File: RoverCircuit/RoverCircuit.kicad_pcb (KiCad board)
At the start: 2 copper layers, 11 parts, among them J1 PIC24_JST_1-10, J2 PIC24_JST_11-20, J3 Servo_JST, J4 Left_Wheel_JST, J5 Right_Wheel_JST, J6 Battery_Terminal, Q1 NMOS, Q2 PMOS, U1 LM2596S-5

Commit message: Added Sharp Sensors to KiCad
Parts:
- removed U1: LM2596S-5, Package_TO_SOT_SMD:TO-263-5_TabPin3
- added D1: LED, LED_THT:LED_D8.0mm, F.Cu at (77.8, 41.0)
- added D2: LED, LED_THT:LED_D8.0mm, F.Cu at (77.8, 51.7)
- added D3: LED, LED_THT:LED_D8.0mm, F.Cu at (77.8, 62.3)
- added D4: LED, LED_THT:LED_D8.0mm, F.Cu at (77.8, 73.0)
- added J10: Front_Sharp_Sensor_JST, Connector_JST:JST_EH_B3B-EH-A_1x03_P2.50mm_Vertical, F.Cu at (54.3, 54.2)
- added J7: Voltage_Regulator_JST, Connector_JST:JST_EH_B3B-EH-A_1x03_P2.50mm_Vertical, F.Cu at (87.9, 54.5)
- added J8: Left_Sharp_Sensor_JST, Connector_JST:JST_EH_B3B-EH-A_1x03_P2.50mm_Vertical, F.Cu at (54.3, 42.5)
- added J9: Right_Sharp_Sensor_JST, Connector_JST:JST_EH_B3B-EH-A_1x03_P2.50mm_Vertical, F.Cu at (54.3, 48.4)
- added R3: 330, Resistor_THT:R_Axial_DIN0207_L6.3mm_D2.5mm_P10.16mm_Horizontal, F.Cu at (85.9, 37.7)
- added R4: 330, Resistor_THT:R_Axial_DIN0207_L6.3mm_D2.5mm_P10.16mm_Horizontal, F.Cu at (85.9, 41.7)
- added R5: 330, Resistor_THT:R_Axial_DIN0207_L6.3mm_D2.5mm_P10.16mm_Horizontal, F.Cu at (85.9, 45.8)
- added R6: 330, Resistor_THT:R_Axial_DIN0207_L6.3mm_D2.5mm_P10.16mm_Horizontal, F.Cu at (85.9, 49.8)
- J6: footprint Connector_Phoenix_SPT:PhoenixContact_SPT_5_1-H-7.5_1x01_P7.5mm_Horizontal -> TerminalBlock_CUI:TerminalBlock_CUI_TB007-508-02_1x02_P5.08mm_Horizontal
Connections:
- J1 pad 1: unconnected-(J1-Pin_1-Pad1) -> Net-(J1-Pin_1)

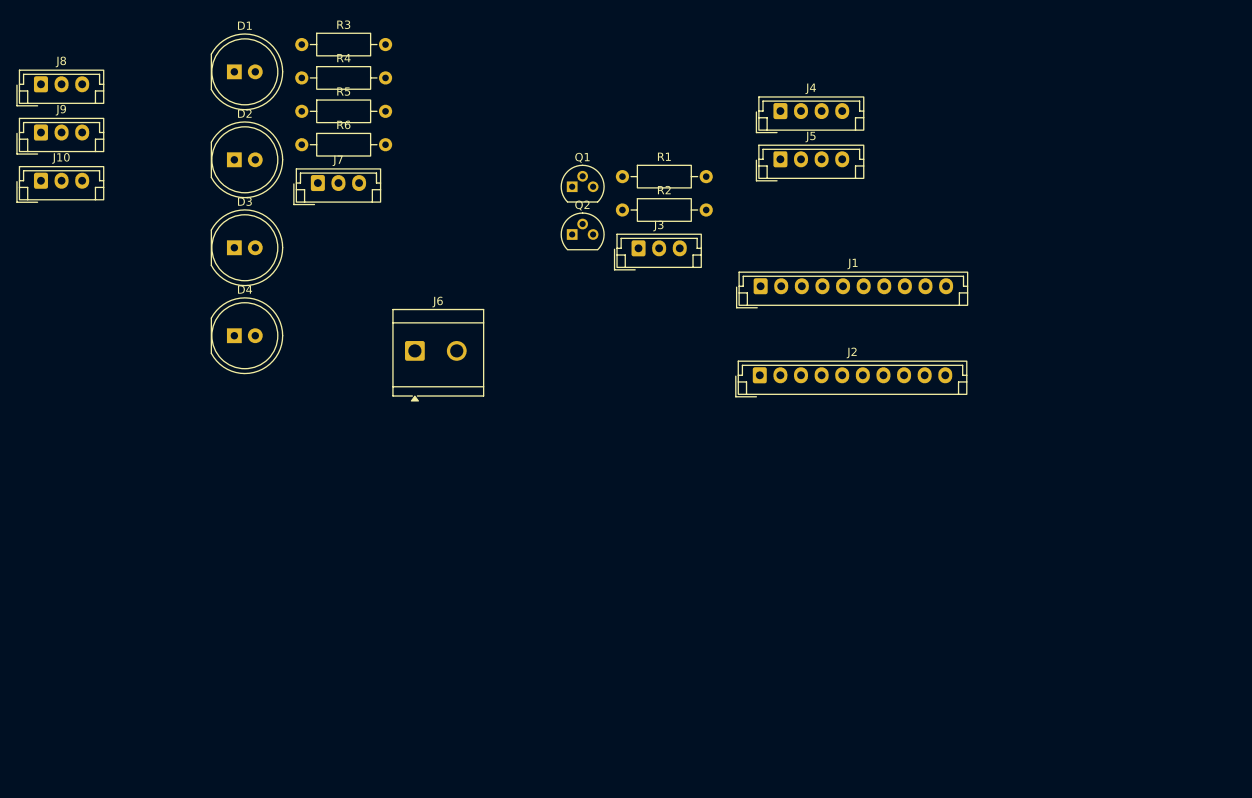
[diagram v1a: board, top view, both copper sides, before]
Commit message: Finalized rover circuit schematic, first version of QRD circuit
rover circuit layout and traces not finished yet
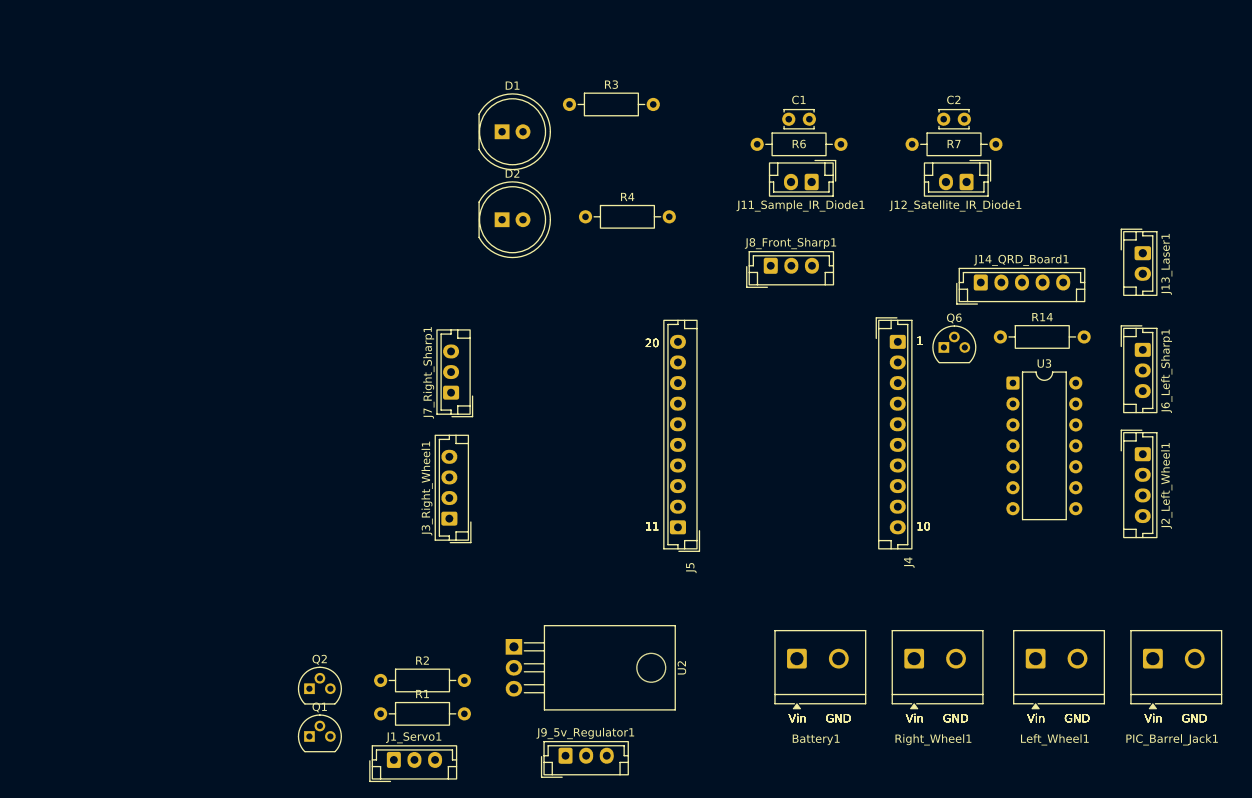
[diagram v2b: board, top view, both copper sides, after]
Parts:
- removed D3, D4: LED, LED_THT:LED_D8.0mm
- removed R5: 330, Resistor_THT:R_Axial_DIN0207_L6.3mm_D2.5mm_P10.16mm_Horizontal
- added C1: 0.1uF, Capacitor_THT:C_Disc_D3.4mm_W2.1mm_P2.50mm, F.Cu at (145.0, 46.7)
- added C2: 0.1uF, Capacitor_THT:C_Disc_D3.4mm_W2.1mm_P2.50mm, F.Cu at (163.8, 46.7)
- added J11_Sample_IR_Diode1: JST_2Pin_P2.54_V, Connector_JST:JST_EH_B2B-EH-A_1x02_P2.50mm_Vertical, F.Cu at (147.8, 54.4)
- added J12_Satellite_IR_Diode1: JST_2Pin_P2.54_V, Connector_JST:JST_EH_B2B-EH-A_1x02_P2.50mm_Vertical, F.Cu at (166.6, 54.4)
- added J13_Laser1: JST_2Pin_P2.54_V, Connector_JST:JST_EH_B2B-EH-A_1x02_P2.50mm_Vertical, F.Cu at (188.0, 63.0)
- added J14_QRD_Board1: JST_5Pin_P2.54_V, Connector_JST:JST_EH_B5B-EH-A_1x05_P2.50mm_Vertical, F.Cu at (168.3, 66.5)
- added Left_Wheel1: Left_Wheel_Power_Terminal, Custom_Library:screw_terminal, F.Cu at (177.7, 112.5)
- added PIC_Barrel_Jack1: PIC_Power_Terminal, Custom_Library:screw_terminal, F.Cu at (191.9, 112.5)
- added Q6: NMOS, Package_TO_SOT_THT:TO-92, F.Cu at (163.8, 74.4)
- added R14: 10kΩ, Resistor_THT:R_Axial_DIN0207_L6.3mm_D2.5mm_P10.16mm_Horizontal, F.Cu at (170.7, 73.2)
- added R7: 1MΩ, Resistor_THT:R_Axial_DIN0207_L6.3mm_D2.5mm_P10.16mm_Horizontal, F.Cu at (160.0, 49.8)
- added Right_Wheel1: Right_Wheel_Terminal, Custom_Library:screw_terminal, F.Cu at (162.9, 112.5)
- added U2: LM1117T-3.3, Package_TO_SOT_THT:TO-220-3_Horizontal_TabDown, F.Cu at (111.7, 110.7)
- added U3: LM324, Package_DIP:DIP-14_W7.62mm, F.Cu at (172.2, 78.7)
- Battery1: renamed from J6; footprint TerminalBlock_CUI:TerminalBlock_CUI_TB007-508-02_1x02_P5.08mm_Horizontal -> Custom_Library:screw_terminal
- J1_Servo1: renamed from J3; value Servo_JST -> JST_3Pin_P2.54_V
- J2_Left_Wheel1: renamed from J4; value Left_Wheel_JST -> JST_4Pin_P2.54_V
- J3_Right_Wheel1: renamed from J5; value Right_Wheel_JST -> JST_4Pin_P2.54_V
- J4: renamed from J1; value PIC24_JST_1-10 -> JST_10Pin_P2.54_V
- J5: renamed from J2; value PIC24_JST_11-20 -> JST_10Pin_P2.54_V
- J6_Left_Sharp1: renamed from J8; value Left_Sharp_Sensor_JST -> JST_3Pin_P2.54_V
- J7_Right_Sharp1: renamed from J9; value Right_Sharp_Sensor_JST -> JST_3Pin_P2.54_V
- J8_Front_Sharp1: renamed from J10; value Front_Sharp_Sensor_JST -> JST_3Pin_P2.54_V
- J9_5v_Regulator1: renamed from J7; value Voltage_Regulator_JST -> JST_3Pin_P2.54_V
- R6: value 330 -> 1MΩ
- moved J6_Left_Sharp1 137.5 mm to (188.0, 74.7), turned to -90 degrees
- moved J8_Front_Sharp1 89.1 mm to (142.8, 64.5)
- moved J9_5v_Regulator1 75.7 mm to (117.9, 124.0)
- moved J1_Servo1 68.8 mm to (97.1, 124.5)
- moved Q1 68.7 mm to (86.9, 121.6)
- moved Q2 68.7 mm to (86.9, 115.8)
- moved R1 67.8 mm to (95.5, 118.9)
- moved R2 67.8 mm to (95.5, 114.8)
- moved Battery1 61.9 mm to (148.7, 112.5)
- moved J2_Left_Wheel1 60.5 mm to (188.0, 87.4), turned to -90 degrees
- moved J3_Right_Wheel1 59.3 mm to (103.8, 95.2), turned to 90 degrees
- moved J7_Right_Sharp1 58.9 mm to (104.0, 79.9), turned to 90 degrees
- moved R6 55.2 mm to (141.2, 49.8)
- moved R4 38.3 mm to (120.4, 58.6)
- moved D1 33.3 mm to (110.2, 48.3)
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- renumbered Q2 to Q1, Q1 to Q2, R2 to R1, R1 to R2
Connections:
- net +3V3 renamed Net-(J5-Pin_10)
- Battery1 pad 1: /9v_Rail -> Net-(Battery1-Pin_1)
- J4 pad 10: /Debug_LED_3 -> /Debug_LED_2
- J4 pad 8: /Debug_LED_1 -> /Right_Of_Line_QRD_Input
- J4 pad 9: /Debug_LED_2 -> /Debug_LED_1
- J5 pad 11: /Debug_LED_4 -> /Laser_Output
- J9_5v_Regulator1 pad 2: /9v_Rail -> /12v_Rail
- R6 pad 1: GND -> Net-(J11_Sample_IR_Diode1-Pin_1)
- R6 pad 2: Net-(D4-K) -> /Sample_Collection_IR_Input
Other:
- board text added: "1"
- board text added: "10"
- board text added: "11"
- board text added: "20"
- board text added: "GND"
- board text added: "Vin"

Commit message: Added low pass filters on every analog input
Used R=150, C=0.1uF to attenuate frequencies above the frequency of how fast the AD converter will read each signal.
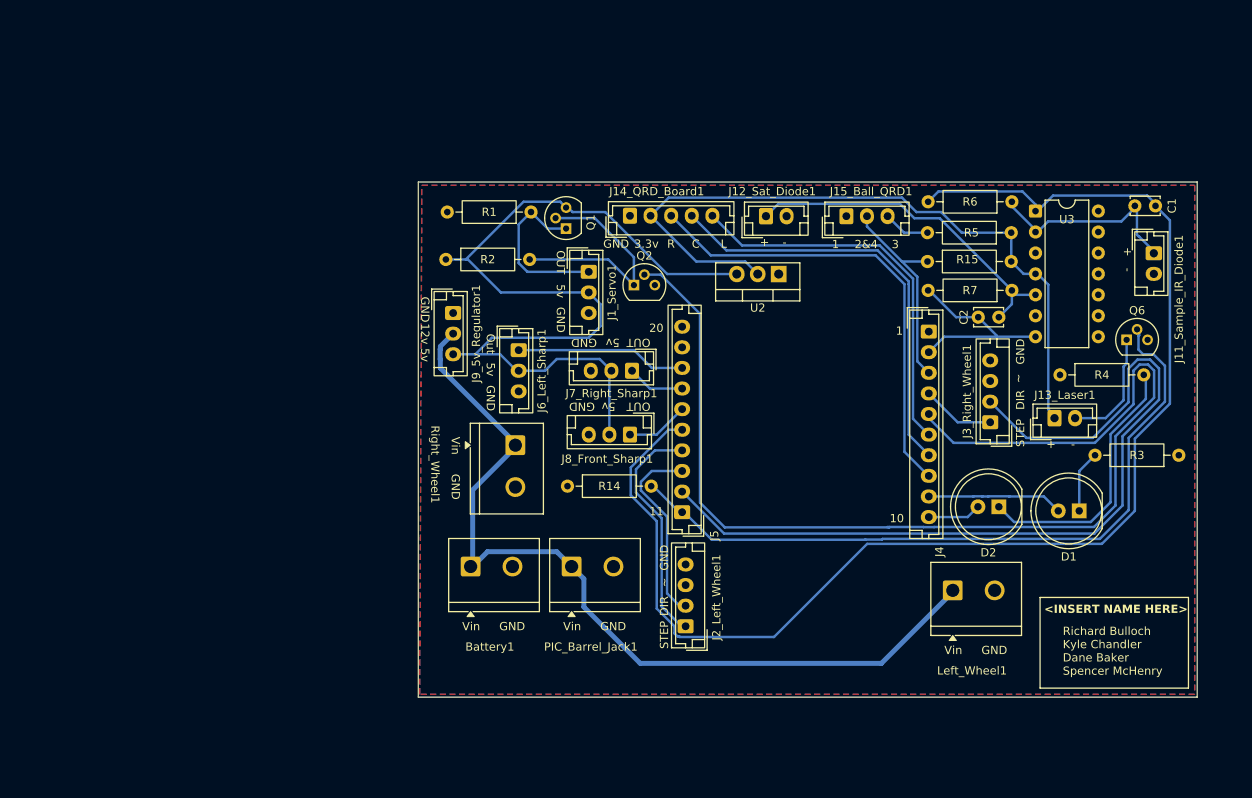
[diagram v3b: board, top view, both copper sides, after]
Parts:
- added J15_Ball_QRD1: JST_3Pin_P2.54_V, Connector_JST:JST_EH_B3B-EH-A_1x03_P2.50mm_Vertical, F.Cu at (152.0, 58.5)
- added R15: 10kΩ, Resistor_THT:R_Axial_DIN0207_L6.3mm_D2.5mm_P10.16mm_Horizontal, F.Cu at (161.8, 64.0)
- added R5: 330Ω, Resistor_THT:R_Axial_DIN0207_L6.3mm_D2.5mm_P10.16mm_Horizontal, F.Cu at (172.0, 60.5)
- U2: footprint Package_TO_SOT_THT:TO-220-3_Horizontal_TabDown -> Package_TO_SOT_THT:TO-220-3_Vertical
- moved R3 85.3 mm to (192.3, 87.5), turned to 180 degrees
- moved D1 83.8 mm to (180.2, 94.2), turned to 180 degrees
- moved J6_Left_Sharp1 75.7 mm to (112.2, 74.8)
- moved PIC_Barrel_Jack1 71.4 mm to (121.4, 101.3)
- moved D2 69.6 mm to (170.5, 93.8), turned to 180 degrees
- moved Q1 69.0 mm to (118.0, 60.0), turned to 90 degrees
- moved J3_Right_Wheel1 66.6 mm to (169.4, 83.5)
- moved J1_Servo1 63.8 mm to (120.8, 65.2), turned to -90 degrees
- moved R1 63.5 mm to (113.8, 58.0), turned to 180 degrees
- moved Q2 62.8 mm to (126.2, 66.9)
- moved R4 60.7 mm to (177.9, 77.8)
- moved J2_Left_Wheel1 59.3 mm to (132.5, 108.2), turned to 90 degrees
- moved Right_Wheel1 56.6 mm to (111.5, 89.0), turned to -90 degrees
- moved R14 55.5 mm to (118.2, 91.2)
- moved U2 55.5 mm to (143.8, 65.5), turned to 180 degrees
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- renumbered J12_Satellite_IR_Diode1 to J12_Sat_Diode1
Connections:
- Battery1 pad 1: Net-(Battery1-Pin_1) -> /12v_Rail
- D1 pad 2: unconnected-(D1-A-Pad2) -> /Debug_LED_1
- D2 pad 2: unconnected-(D2-A-Pad2) -> /Debug_LED_2
- J1_Servo1 pad 1: /5v_Rail -> Net-(J1_Servo1-Pin_1)
- Q1 pad 1: Net-(Q1-D) -> Net-(J1_Servo1-Pin_1)
- R1 pad 1: Net-(Q1-D) -> Net-(J1_Servo1-Pin_1)
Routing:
- net /Sample_Collection_IR_Input: track 0.00 -> 163.1 mm
- net /Servo_PWM: track 0.00 -> 138.7 mm
- net /5v_Rail: track 0.00 -> 109.1 mm
- net /12v_Rail: track 0.00 -> 105.5 mm
- net /Right_Wheel_DIR: track 0.00 -> 104.5 mm
- net /3.3v_Rail: track 0.00 -> 87.8 mm
- net /Laser_Output: track 0.00 -> 87.7 mm
- net /Right_Of_Line_QRD_Input: track 0.00 -> 56.2 mm
- net /On_Line_QRD_Input: track 0.00 -> 51.7 mm
- net /Left_Of_Line_QRD_Input: track 0.00 -> 47.2 mm
- net Net-(J12_Sat_Diode1-Pin_1): track 0.00 -> 42.1 mm
- net Net-(D2-K): track 0.00 -> 32.5 mm
- net /Left_Wheel_Step: track 0.00 -> 28.8 mm
- net Net-(Q1-G): track 0.00 -> 28.5 mm
- net /Ball_Color_QRD_Input: track 0.00 -> 25.2 mm
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- added copper zone on B.Cu, net GND
- added copper zone on F.Cu, net GND
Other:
- board outline added: 94.5 x 62.5 mm
- board text added: "<INSERT NAME HERE>"
- board text added: "Richard Bulloch Kyle Chandler Dane Baker Spencer McHenry"
- board text removed: "1"
- board text removed: "10"
- board text removed: "11"
- board text removed: "20"
- board text removed: "GND"
- board text removed: "Vin"

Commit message: Added signal conditioning and reorganized the PCB
Also added bulk capacitors on each power rail
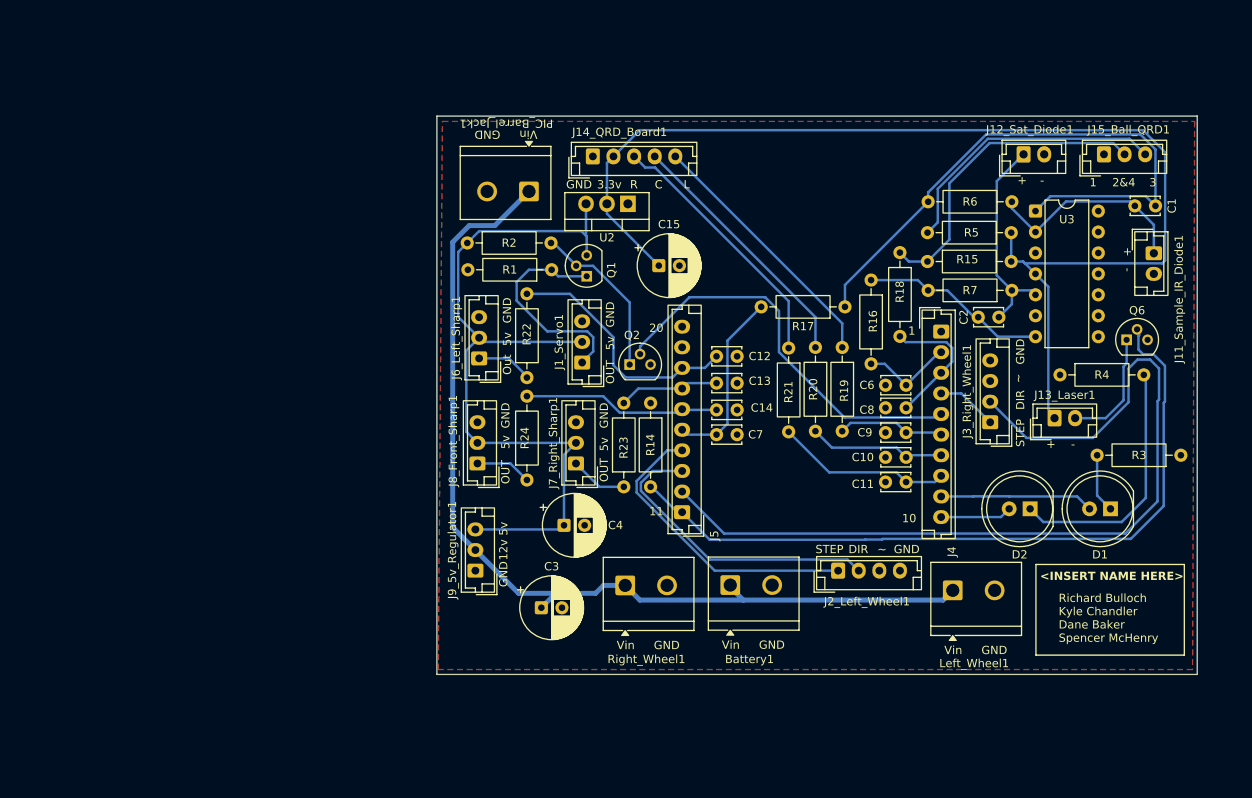
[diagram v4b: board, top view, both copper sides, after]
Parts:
- added C10: 0.1uF, Capacitor_THT:C_Disc_D3.4mm_W2.1mm_P2.50mm, F.Cu at (159.2, 87.8)
- added C11: 0.1uF, Capacitor_THT:C_Disc_D3.4mm_W2.1mm_P2.50mm, F.Cu at (159.2, 90.8)
- added C12: 0.1uF, Capacitor_THT:C_Disc_D3.4mm_W2.1mm_P2.50mm, F.Cu at (136.2, 75.5)
- added C13: 0.1uF, Capacitor_THT:C_Disc_D3.4mm_W2.1mm_P2.50mm, F.Cu at (136.2, 78.8)
- added C14: 0.1uF, Capacitor_THT:C_Disc_D3.4mm_W2.1mm_P2.50mm, F.Cu at (136.2, 82.0)
- added C15: 100uF, Capacitor_THT:CP_Radial_D7.5mm_P2.50mm, F.Cu at (129.2, 64.5)
- added C3: 100uF, Capacitor_THT:CP_Radial_D7.5mm_P2.50mm, F.Cu at (115.0, 106.0)
- added C4: 100uF, Capacitor_THT:CP_Radial_D7.5mm_P2.50mm, F.Cu at (117.8, 96.0)
- added C6: 0.1uF, Capacitor_THT:C_Disc_D3.4mm_W2.1mm_P2.50mm, F.Cu at (159.2, 79.0)
- added C7: 0.1uF, Capacitor_THT:C_Disc_D3.4mm_W2.1mm_P2.50mm, F.Cu at (136.2, 85.0)
- added C8: 0.1uF, Capacitor_THT:C_Disc_D3.4mm_W2.1mm_P2.50mm, F.Cu at (159.2, 81.8)
- added C9: 0.1uF, Capacitor_THT:C_Disc_D3.4mm_W2.1mm_P2.50mm, F.Cu at (159.2, 84.8)
- added R16: 150Ω, Resistor_THT:R_Axial_DIN0207_L6.3mm_D2.5mm_P10.16mm_Horizontal, F.Cu at (155.0, 66.2)
- added R17: 150Ω, Resistor_THT:R_Axial_DIN0207_L6.3mm_D2.5mm_P10.16mm_Horizontal, F.Cu at (151.8, 69.5)
- added R18: 150Ω, Resistor_THT:R_Axial_DIN0207_L6.3mm_D2.5mm_P10.16mm_Horizontal, F.Cu at (158.5, 62.9)
- added R19: 150Ω, Resistor_THT:R_Axial_DIN0207_L6.3mm_D2.5mm_P10.16mm_Horizontal, F.Cu at (151.5, 74.4)
- added R20: 150Ω, Resistor_THT:R_Axial_DIN0207_L6.3mm_D2.5mm_P10.16mm_Horizontal, F.Cu at (148.2, 74.4)
- added R21: 150Ω, Resistor_THT:R_Axial_DIN0207_L6.3mm_D2.5mm_P10.16mm_Horizontal, F.Cu at (145.0, 74.5)
- added R22: 150Ω, Resistor_THT:R_Axial_DIN0207_L6.3mm_D2.5mm_P10.16mm_Horizontal, F.Cu at (113.2, 78.1)
- added R23: 150Ω, Resistor_THT:R_Axial_DIN0207_L6.3mm_D2.5mm_P10.16mm_Horizontal, F.Cu at (125.0, 91.3)
- added R24: 150Ω, Resistor_THT:R_Axial_DIN0207_L6.3mm_D2.5mm_P10.16mm_Horizontal, F.Cu at (113.2, 90.5)
- moved PIC_Barrel_Jack1 47.4 mm to (110.8, 55.1), turned to 180 degrees
- moved J12_Sat_Diode1 32.1 mm to (173.5, 51.0)
- moved J15_Ball_QRD1 32.1 mm to (183.2, 51.0)
- moved Battery1 31.6 mm to (140.6, 103.6)
- moved J9_5v_Regulator1 31.4 mm to (107.0, 101.5), turned to 90 degrees
- moved Right_Wheel1 22.0 mm to (127.9, 103.6), turned to 0 degrees
- moved U2 20.2 mm to (125.5, 57.0)
- moved J2_Left_Wheel1 19.7 mm to (151.0, 101.5), turned to 0 degrees
- moved J8_Front_Sharp1 18.8 mm to (107.2, 88.5), turned to 90 degrees
- moved R14 14.3 mm to (128.2, 81.2), turned to -90 degrees
- moved J7_Right_Sharp1 13.1 mm to (119.2, 88.5), turned to 90 degrees
- moved J1_Servo1 11.0 mm to (120.0, 76.2), turned to 90 degrees
- moved Q2 9.65 mm to (125.7, 76.5)
- moved J14_QRD_Board1 8.49 mm to (121.2, 51.2)
- moved R1 7.43 mm to (116.2, 65.0)
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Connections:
- C1 pad 2: /Sample_Collection_IR_Input -> /Sample_Collection_IR_Output
- C2 pad 2: /Satellite_IR_Input -> /Satellite_IR_Output
- J14_QRD_Board1 pad 3: /Right_Of_Line_QRD_Input -> /Right_Of_Line_QRD_Output
- J14_QRD_Board1 pad 4: /On_Line_QRD_Input -> /On_Line_QRD_Output
- J14_QRD_Board1 pad 5: /Left_Of_Line_QRD_Input -> /Left_Of_Line_QRD_Output
- J15_Ball_QRD1 pad 2: /Ball_Color_QRD_Input -> /Ball_Color_QRD_Output
- J6_Left_Sharp1 pad 1: /Left_Sharp_Input -> /Left_Sharp_Output
- J7_Right_Sharp1 pad 1: /Right_Sharp_Input -> /Right_Sharp_Output
- J8_Front_Sharp1 pad 1: /Front_Sharp_Input -> /Front_Sharp_Output
- R15 pad 1: /Ball_Color_QRD_Input -> /Ball_Color_QRD_Output
- R6 pad 2: /Sample_Collection_IR_Input -> /Sample_Collection_IR_Output
- R7 pad 2: /Satellite_IR_Input -> /Satellite_IR_Output
- U3 pad 1: /Sample_Collection_IR_Input -> /Sample_Collection_IR_Output
- U3 pad 7: /Satellite_IR_Input -> /Satellite_IR_Output
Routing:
- net /Sample_Collection_IR_Input: track 163.1 -> 22.2 mm
- net /Servo_PWM: track 138.7 -> 49.1 mm
- net /Sample_Collection_IR_Output: track 0.00 -> 71.9 mm
- net /3.3v_Rail: track 87.8 -> 141.3 mm
- net /Ball_Color_QRD_Output: track 0.00 -> 38.2 mm
- net /On_Line_QRD_Input: track 51.7 -> 16.7 mm
- net /Right_Of_Line_QRD_Input: track 56.2 -> 21.3 mm
- net /Left_Of_Line_QRD_Input: track 47.2 -> 13.0 mm
- net /Right_Of_Line_QRD_Output: track 0.00 -> 31.7 mm
- net /Left_Of_Line_QRD_Output: track 0.00 -> 31.6 mm
- net /On_Line_QRD_Output: track 0.00 -> 31.2 mm
- net Net-(J15_Ball_QRD1-Pin_3): track 5.67 -> 34.3 mm
- net /Satellite_IR_Output: track 0.00 -> 22.8 mm
- net Net-(J12_Sat_Diode1-Pin_1): track 42.1 -> 25.6 mm
- net /Front_Sharp_Input: track 7.61 -> 24.0 mm
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- removed copper zone on B.Cu, net GND
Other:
- board size 94.5 x 62.5 mm -> 92.2 x 67.7 mm
